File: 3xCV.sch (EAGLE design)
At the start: 90 parts, among them IC1 TL074, IC2 TL074, IC3 TL074, SW1 TL2285

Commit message: Somewhat modified. No thru jacks (out of space). Aligned input jacks with outputs.
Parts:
- removed R17, R30, R45: 220, rcl:R-US_R0603
- removed SW1: TL2285, lb_devs:TL2285
- removed THRU, THRU1, THRU2: WQP-PJ301M-12_JACK, thonkiconn:WQP-PJ301M-12_JACK
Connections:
- removed net N$18: R17.2, THRU.2
- removed net N$38: R30.2, THRU1.2
- removed net N$55: R45.2, THRU2.2
- net GND: no longer THRU.1, THRU1.1, THRU2.1
- net MIX1: no longer SW1.P3
- net MIX2: no longer SW1.P2
- net N$25: no longer R30.1
- net N$42: no longer R45.1
- net N$5: no longer R17.1
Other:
- note removed: "Switch connect signal mix circuit of units 1 and 2."
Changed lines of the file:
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@@
 <part name="R15" library="rcl" deviceset="R-US_" device="R0603" value="100k"/>
 <part name="R16" library="rcl" deviceset="R-US_" device="R0603" value="100k"/>
-<part name="THRU" library="thonkiconn" deviceset="WQP-PJ301M-12_JACK" device=""/>
-<part name="GND7" library="supply1" deviceset="GND" device=""/>
-<part name="R17" library="rcl" deviceset="R-US_" device="R0603" value="220"/>
 <part name="JP1" library="pinhead" deviceset="PINHD-2X5" device=""/>
 <part name="D1" library="diode" deviceset="DIODE-" device="DO214AA" value="diode"/>
@@
 <part name="R28" library="rcl" deviceset="R-US_" device="R0603" value="100k"/>
 <part name="R29" library="rcl" deviceset="R-US_" device="R0603" value="100k"/>
-<part name="THRU1" library="thonkiconn" deviceset="WQP-PJ301M-12_JACK" device=""/>
-<part name="GND16" library="supply1" deviceset="GND" device=""/>
-<part name="R30" library="rcl" deviceset="R-US_" device="R0603" value="220"/>
 <part name="GND17" library="supply1" deviceset="GND" device=""/>
 <part name="IC3" library="linear" deviceset="LM324" device="D" value="TL074"/>
@@
 <part name="R43" library="rcl" deviceset="R-US_" device="R0603" value="100k"/>
 <part name="R44" library="rcl" deviceset="R-US_" device="R0603" value="100k"/>
-<part name="THRU2" library="thonkiconn" deviceset="WQP-PJ301M-12_JACK" device=""/>
-<part name="GND24" library="supply1" deviceset="GND" device=""/>
-<part name="R45" library="rcl" deviceset="R-US_" device="R0603" value="220"/>
 <part name="GND25" library="supply1" deviceset="GND" device=""/>
 <part name="OUT3" library="thonkiconn" deviceset="WQP-PJ301M-12_JACK" device=""/>
@@
 <part name="R50" library="rcl" deviceset="R-US_" device="R0603" value="100k"/>
 <part name="R51" library="rcl" deviceset="R-US_" device="R0603" value="100k"/>
-<part name="SW1" library="lb_devs" deviceset="TL2285" device=""/>
 </parts>
 <sheets>
 <sheet>
 <plain>
-<text x="254" y="193.04" size="1.778" layer="91">Switch connect signal mix circuit of units 1 and 2.</text>
 </plain>
 <instances>
@@
 <instance part="R15" gate="G$1" x="139.7" y="48.26" rot="R180"/>
 <instance part="R16" gate="G$1" x="139.7" y="27.94" rot="R180"/>
-<instance part="THRU" gate="G$1" x="223.52" y="86.36"/>
-<instance part="GND7" gate="1" x="213.36" y="76.2"/>
-<instance part="R17" gate="G$1" x="205.74" y="88.9"/>
 <instance part="JP1" gate="A" x="284.48" y="238.76"/>
 <instance part="D1" gate="G$1" x="309.88" y="251.46"/>
@@
 <instance part="R28" gate="G$1" x="139.7" y="127" rot="R180"/>
 <instance part="R29" gate="G$1" x="139.7" y="106.68" rot="R180"/>
-<instance part="THRU1" gate="G$1" x="223.52" y="165.1"/>
-<instance part="GND16" gate="1" x="213.36" y="154.94"/>
-<instance part="R30" gate="G$1" x="205.74" y="167.64"/>
 <instance part="GND17" gate="1" x="45.72" y="116.84"/>
 <instance part="IC3" gate="A" x="88.9" y="236.22"/>
@@
 <instance part="R43" gate="G$1" x="139.7" y="205.74" rot="R180"/>
 <instance part="R44" gate="G$1" x="139.7" y="185.42" rot="R180"/>
-<instance part="THRU2" gate="G$1" x="223.52" y="243.84"/>
-<instance part="GND24" gate="1" x="213.36" y="233.68"/>
-<instance part="R45" gate="G$1" x="205.74" y="246.38"/>
 <instance part="GND25" gate="1" x="45.72" y="195.58"/>
 <instance part="OUT3" gate="G$1" x="256.54" y="144.78"/>
@@
 <instance part="R50" gate="G$1" x="187.96" y="134.62" rot="R180"/>
 <instance part="R51" gate="G$1" x="187.96" y="55.88" rot="R180"/>
-<instance part="SW1" gate="G$1" x="281.94" y="177.8"/>
 </instances>
 <busses>
@@
 <wire x1="109.22" y1="68.58" x2="109.22" y2="78.74" width="0.1524" layer="91"/>
 <junction x="101.6" y="78.74"/>
-<pinref part="R17" gate="G$1" pin="1"/>
-<wire x1="200.66" y1="88.9" x2="109.22" y2="88.9" width="0.1524" layer="91"/>
-<wire x1="109.22" y1="88.9" x2="109.22" y2="78.74" width="0.1524" layer="91"/>
-<junction x="109.22" y="78.74"/>
 </segment>
 </net>
@@
 <wire x1="180.34" y1="30.48" x2="180.34" y2="27.94" width="0.1524" layer="91"/>
 <pinref part="GND6" gate="1" pin="GND"/>
-</segment>
-<segment>
-<pinref part="THRU" gate="G$1" pin="1"/>
-<wire x1="218.44" y1="83.82" x2="213.36" y2="83.82" width="0.1524" layer="91"/>
-<pinref part="GND7" gate="1" pin="GND"/>
-<wire x1="213.36" y1="83.82" x2="213.36" y2="78.74" width="0.1524" layer="91"/>
 </segment>
 <segment>
@@
 </segment>
 <segment>
-<pinref part="THRU1" gate="G$1" pin="1"/>
-<wire x1="218.44" y1="162.56" x2="213.36" y2="162.56" width="0.1524" layer="91"/>
-<pinref part="GND16" gate="1" pin="GND"/>
-<wire x1="213.36" y1="162.56" x2="213.36" y2="157.48" width="0.1524" layer="91"/>
-</segment>
-<segment>
 <pinref part="C7" gate="G$1" pin="2"/>
 <pinref part="C8" gate="G$1" pin="1"/>
@@
 <wire x1="180.34" y1="187.96" x2="180.34" y2="185.42" width="0.1524" layer="91"/>
 <pinref part="GND23" gate="1" pin="GND"/>
-</segment>
-<segment>
-<pinref part="THRU2" gate="G$1" pin="1"/>
-<wire x1="218.44" y1="241.3" x2="213.36" y2="241.3" width="0.1524" layer="91"/>
-<pinref part="GND24" gate="1" pin="GND"/>
-<wire x1="213.36" y1="241.3" x2="213.36" y2="236.22" width="0.1524" layer="91"/>
 </segment>
 <segment>
@@
 </segment>
 </net>
-<net name="N$18" class="0">
-<segment>
-<pinref part="THRU" gate="G$1" pin="2"/>
-<pinref part="R17" gate="G$1" pin="2"/>
-<wire x1="218.44" y1="88.9" x2="210.82" y2="88.9" width="0.1524" layer="91"/>
-</segment>
-</net>
 <net name="N$20" class="0">
 <segment>
@@
 <wire x1="109.22" y1="147.32" x2="109.22" y2="157.48" width="0.1524" layer="91"/>
 <junction x="101.6" y="157.48"/>
-<pinref part="R30" gate="G$1" pin="1"/>
-<wire x1="200.66" y1="167.64" x2="109.22" y2="167.64" width="0.1524" layer="91"/>
-<wire x1="109.22" y1="167.64" x2="109.22" y2="157.48" width="0.1524" layer="91"/>
-<junction x="109.22" y="157.48"/>
 </segment>
 </net>
@@
 <wire x1="157.48" y1="116.84" x2="157.48" y2="139.7" width="0.1524" layer="91"/>
 <junction x="157.48" y="139.7"/>
-<wire x1="157.48" y1="160.02" x2="165.1" y2="160.02" width="0.1524" layer="91"/>
-<junction x="157.48" y="160.02"/>
-<label x="165.1" y="160.02" size="1.778" layer="95"/>
-</segment>
-<segment>
-<pinref part="SW1" gate="G$1" pin="P2"/>
-<wire x1="289.56" y1="180.34" x2="299.72" y2="180.34" width="0.1524" layer="91"/>
-<label x="299.72" y="180.34" size="1.778" layer="95"/>
 </segment>
 </net>
@@
 </segment>
 </net>
-<net name="N$38" class="0">
-<segment>
-<pinref part="THRU1" gate="G$1" pin="2"/>
-<pinref part="R30" gate="G$1" pin="2"/>
-<wire x1="218.44" y1="167.64" x2="210.82" y2="167.64" width="0.1524" layer="91"/>
-</segment>
-</net>
 <net name="N$39" class="0">
 <segment>
@@
 <wire x1="109.22" y1="226.06" x2="109.22" y2="236.22" width="0.1524" layer="91"/>
 <junction x="101.6" y="236.22"/>
-<pinref part="R45" gate="G$1" pin="1"/>
-<wire x1="200.66" y1="246.38" x2="109.22" y2="246.38" width="0.1524" layer="91"/>
-<wire x1="109.22" y1="246.38" x2="109.22" y2="236.22" width="0.1524" layer="91"/>
-<junction x="109.22" y="236.22"/>
 </segment>
 </net>
@@
 <wire x1="157.48" y1="195.58" x2="157.48" y2="218.44" width="0.1524" layer="91"/>
 <junction x="157.48" y="218.44"/>
-<wire x1="157.48" y1="238.76" x2="165.1" y2="238.76" width="0.1524" layer="91"/>
-<junction x="157.48" y="238.76"/>
-<label x="165.1" y="238.76" size="1.778" layer="95"/>
-</segment>
-<segment>
-<pinref part="SW1" gate="G$1" pin="P3"/>
-<wire x1="274.32" y1="182.88" x2="264.16" y2="182.88" width="0.1524" layer="91"/>
-<label x="264.16" y="182.88" size="1.778" layer="95" rot="R180"/>
 </segment>
 </net>
@@
 </segment>
 </net>
-<net name="N$55" class="0">
-<segment>
-<pinref part="THRU2" gate="G$1" pin="2"/>
-<pinref part="R45" gate="G$1" pin="2"/>
-<wire x1="218.44" y1="246.38" x2="210.82" y2="246.38" width="0.1524" layer="91"/>
-</segment>
-</net>

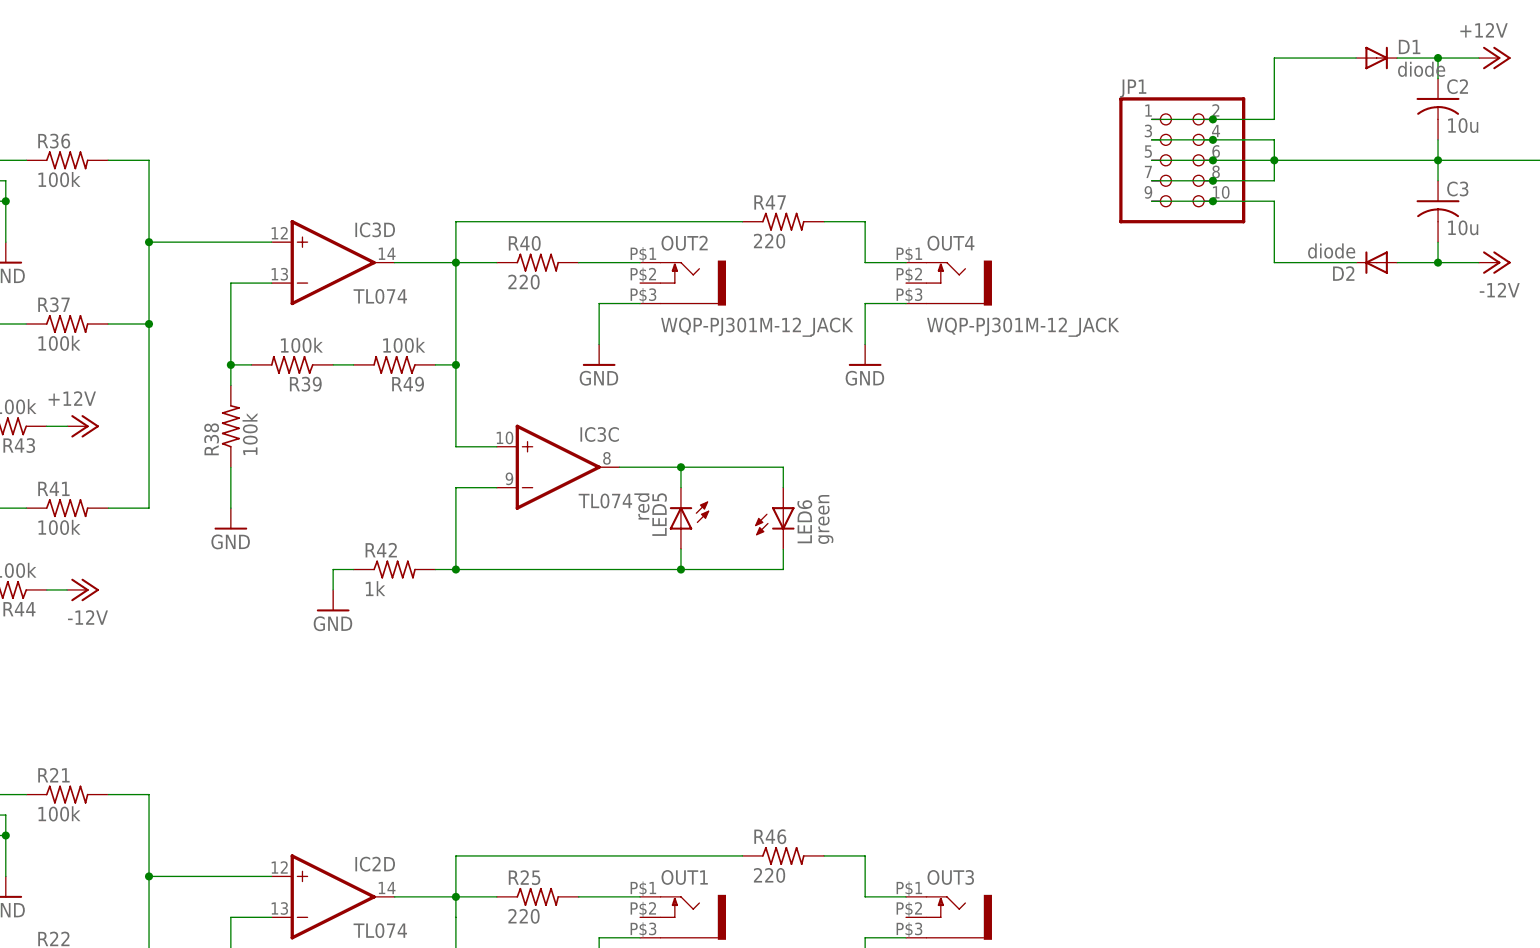
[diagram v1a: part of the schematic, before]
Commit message: Added back 1+2 mix button. There is room for it. Yay! =)
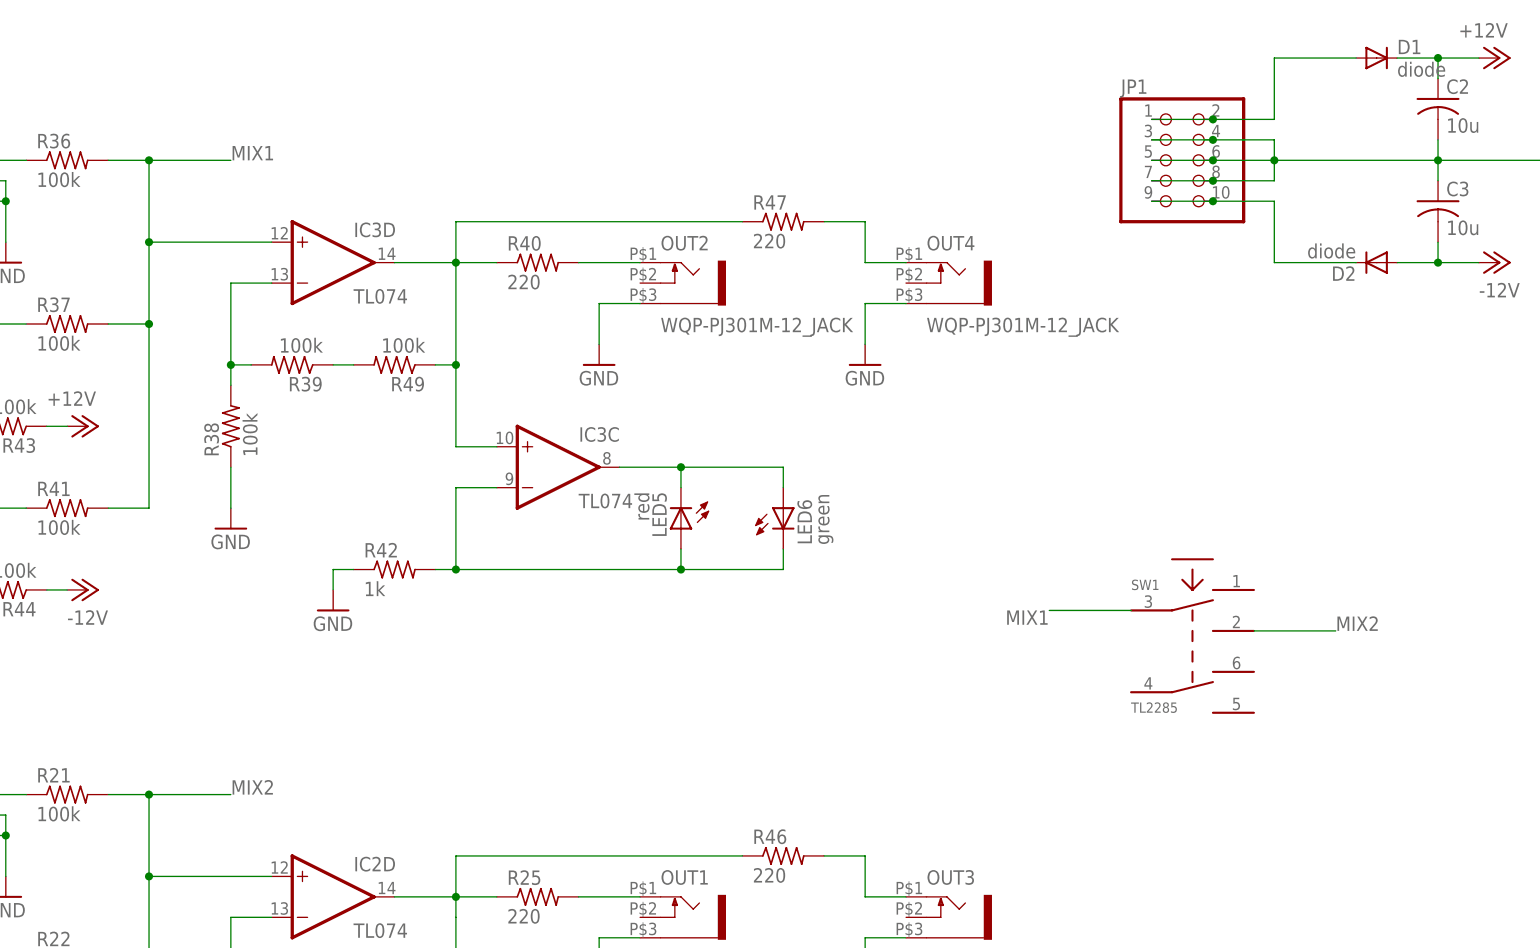
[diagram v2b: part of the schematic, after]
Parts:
- added SW1: TL2285, lb_devs:TL2285
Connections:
- net MIX1: now also SW1.P3
- net MIX2: now also SW1.P2
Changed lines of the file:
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@@
 <part name="R50" library="rcl" deviceset="R-US_" device="R0603" value="100k"/>
 <part name="R51" library="rcl" deviceset="R-US_" device="R0603" value="100k"/>
+<part name="SW1" library="lb_devs" deviceset="TL2285" device=""/>
 </parts>
 <sheets>
@@
 <instance part="R50" gate="G$1" x="187.96" y="134.62" rot="R180"/>
 <instance part="R51" gate="G$1" x="187.96" y="55.88" rot="R180"/>
+<instance part="SW1" gate="G$1" x="287.02" y="177.8"/>
 </instances>
 <busses>
@@
 <wire x1="157.48" y1="116.84" x2="157.48" y2="139.7" width="0.1524" layer="91"/>
 <junction x="157.48" y="139.7"/>
+<wire x1="157.48" y1="160.02" x2="167.64" y2="160.02" width="0.1524" layer="91"/>
+<junction x="157.48" y="160.02"/>
+<label x="167.64" y="160.02" size="1.778" layer="95"/>
+</segment>
+<segment>
+<pinref part="SW1" gate="G$1" pin="P2"/>
+<wire x1="294.64" y1="180.34" x2="304.8" y2="180.34" width="0.1524" layer="91"/>
+<label x="304.8" y="180.34" size="1.778" layer="95"/>
 </segment>
 </net>
@@
 <wire x1="157.48" y1="195.58" x2="157.48" y2="218.44" width="0.1524" layer="91"/>
 <junction x="157.48" y="218.44"/>
-</segment>
-</net>
+<wire x1="157.48" y1="238.76" x2="167.64" y2="238.76" width="0.1524" layer="91"/>
+<junction x="157.48" y="238.76"/>
+<label x="167.64" y="238.76" size="1.778" layer="95"/>
+</segment>
+<segment>
+<pinref part="SW1" gate="G$1" pin="P3"/>
+<wire x1="279.4" y1="182.88" x2="269.24" y2="182.88" width="0.1524" layer="91"/>
+<label x="269.24" y="182.88" size="1.778" layer="95" rot="R180"/>
+</segment>
+</net>

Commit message: Added thru switch in unit 1, can switch output 1 to provide buffered output of unchanged input signal.
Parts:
- added SW2: TL2285, lb_devs:TL2285
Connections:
- new net N$18: R47.1, SW2.P4
- net N$42: now also SW2.P5
- net N$47: now also SW2.P6; no longer R47.1
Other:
- note added: "Switch connects CV mix of unit 1 and 2."
- moved on the sheet: R47
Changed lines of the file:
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@@
 <part name="R51" library="rcl" deviceset="R-US_" device="R0603" value="100k"/>
 <part name="SW1" library="lb_devs" deviceset="TL2285" device=""/>
+<part name="SW2" library="lb_devs" deviceset="TL2285" device=""/>
 </parts>
 <sheets>
 <sheet>
 <plain>
+<text x="266.7" y="190.5" size="1.778" layer="91">Switch connects CV mix of unit 1 and 2.</text>
 </plain>
 <instances>
@@
 <instance part="GND26" gate="1" x="246.38" y="134.62"/>
 <instance part="OUT4" gate="G$1" x="256.54" y="223.52"/>
-<instance part="R47" gate="G$1" x="236.22" y="231.14"/>
+<instance part="R47" gate="G$1" x="236.22" y="238.76"/>
 <instance part="GND27" gate="1" x="246.38" y="213.36"/>
 <instance part="OUT5" gate="G$1" x="256.54" y="66.04"/>
@@
 <instance part="R51" gate="G$1" x="187.96" y="55.88" rot="R180"/>
 <instance part="SW1" gate="G$1" x="287.02" y="177.8"/>
+<instance part="SW2" gate="G$1" x="215.9" y="243.84" rot="MR0"/>
 </instances>
 <busses>
@@
 <wire x1="109.22" y1="226.06" x2="109.22" y2="236.22" width="0.1524" layer="91"/>
 <junction x="101.6" y="236.22"/>
+<pinref part="SW2" gate="G$1" pin="P5"/>
+<wire x1="208.28" y1="236.22" x2="200.66" y2="236.22" width="0.1524" layer="91"/>
+<wire x1="200.66" y1="236.22" x2="200.66" y2="246.38" width="0.1524" layer="91"/>
+<wire x1="200.66" y1="246.38" x2="109.22" y2="246.38" width="0.1524" layer="91"/>
+<wire x1="109.22" y1="246.38" x2="109.22" y2="236.22" width="0.1524" layer="91"/>
+<junction x="109.22" y="236.22"/>
 </segment>
 </net>
@@
 <pinref part="IC3" gate="C" pin="+IN"/>
 <wire x1="195.58" y1="203.2" x2="200.66" y2="203.2" width="0.1524" layer="91"/>
-<pinref part="R47" gate="G$1" pin="1"/>
-<wire x1="231.14" y1="231.14" x2="195.58" y2="231.14" width="0.1524" layer="91"/>
-<wire x1="195.58" y1="231.14" x2="195.58" y2="226.06" width="0.1524" layer="91"/>
 <pinref part="R49" gate="G$1" pin="1"/>
 <wire x1="193.04" y1="213.36" x2="195.58" y2="213.36" width="0.1524" layer="91"/>
 <junction x="195.58" y="213.36"/>
+<pinref part="SW2" gate="G$1" pin="P6"/>
+<wire x1="208.28" y1="241.3" x2="195.58" y2="241.3" width="0.1524" layer="91"/>
+<wire x1="195.58" y1="241.3" x2="195.58" y2="226.06" width="0.1524" layer="91"/>
 </segment>
 </net>
@@
 <segment>
 <pinref part="R47" gate="G$1" pin="2"/>
-<wire x1="241.3" y1="231.14" x2="246.38" y2="231.14" width="0.1524" layer="91"/>
-<wire x1="246.38" y1="231.14" x2="246.38" y2="226.06" width="0.1524" layer="91"/>
+<wire x1="241.3" y1="238.76" x2="246.38" y2="238.76" width="0.1524" layer="91"/>
+<wire x1="246.38" y1="238.76" x2="246.38" y2="226.06" width="0.1524" layer="91"/>
 <pinref part="OUT4" gate="G$1" pin="2"/>
 <wire x1="246.38" y1="226.06" x2="251.46" y2="226.06" width="0.1524" layer="91"/>
@@
 </segment>
 </net>
+<net name="N$18" class="0">
+<segment>
+<pinref part="SW2" gate="G$1" pin="P4"/>
+<pinref part="R47" gate="G$1" pin="1"/>
+<wire x1="223.52" y1="238.76" x2="231.14" y2="238.76" width="0.1524" layer="91"/>
+</segment>
+</net>
